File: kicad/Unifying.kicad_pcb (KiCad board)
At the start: 4 copper layers, 115.1 x 61 mm, 119 parts, among them J1 Conn_01x02, J10 HDMI_C_1.4, J11 HDMI_C_1.4, J12 nRpiBoot, J13 Conn_01x03, J14 Conn_01x03, J15 AudioOUT, J16 Micro_SD_Card_Det, J17 THD-20-R, J18 GLOBAL_EN, J19 AudioAMP, J2 Bus_M.2_Socket_B, J3 USB_OTG, J4 Conn_01x04_Male, J5 USB_A, J6 USB_A, J7 USB_MICRO, J8 Conn_01x22_Female, J9 Conn_01x22_Female, Q1 DMP3013SFV-7, U10 74LVC1G07SE-7, U11 RT9742GGJ5, U2 AP64501SP-13, U3 FSUSB42MUX, U4 USB2514B-I/M2, U6 AP22653W6, U7 RT9742SNGV, U8 74LVC1G07SE-7, U9 NC7WZ16, Y1 24MHz

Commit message: Adding changes to PCB, routing board
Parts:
- added R2: DNP, Resistor_SMD:R_0402_1005Metric, F.Cu at (123.3, 95.0)
- J10: value HDMI_C_1.4 -> GPDI0; footprint CM4IO:EDAC 690-019-298-412 -> hdmi-d:CONN-10029449-111RLF
- J11: value HDMI_C_1.4 -> GPDI1; footprint CM4IO:EDAC 690-019-298-412 -> hdmi-d:CONN-10029449-111RLF
- moved J11 2.65 mm to (128.4, 86.6)
- moved J10 1.81 mm to (104.5, 88.6)
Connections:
- net /CM4_HighSpeed/HDMI0_CK_N renamed HDMI0_CK_N
- net /CM4_HighSpeed/HDMI0_D0_N renamed HDMI0_D0_N
- net /CM4_HighSpeed/HDMI0_D1_N renamed HDMI0_D1_N
- net /CM4_HighSpeed/HDMI0_D2_N renamed HDMI0_D2_N
- net /CM4_HighSpeed/HDMI0_HOTPLUG renamed HDMI0_HOTPLUG
- net /CM4_HighSpeed/HDMI0_SCL renamed HDMI0_SCL
- net /CM4_HighSpeed/HDMI0_SDA renamed HDMI0_SDA
- net /CM4_HighSpeed/HDMI_5v renamed HDMI_5v
- J10 pad 1: GND -> HDMI0_D2_P
- J10 pad 10: GND -> HDMI0_CK_P
- J10 pad 11: /CM4_HighSpeed/HDMI0_CK_P -> GND
- J10 pad 13: GND -> HDMI0_CEC
- J10 pad 14: /CM4_HighSpeed/HDMI0_CEC -> unconnected-(J10-P14)
- J10 pad 17: unconnected-(J10-UTILITY/HEAC+) -> GND
- J10 pad 2: /CM4_HighSpeed/HDMI0_D2_P -> GND
- J10 pad 4: GND -> HDMI0_D1_P
- J10 pad 5: /CM4_HighSpeed/HDMI0_D1_P -> GND
- J10 pad 7: GND -> HDMI0_D0_P
- J10 pad 8: /CM4_HighSpeed/HDMI0_D0_P -> GND
- J11 pad 1: GND -> /CM4_HighSpeed/HDMI1_D2_P
- J11 pad 10: GND -> /CM4_HighSpeed/HDMI1_CK_P
- J11 pad 11: /CM4_HighSpeed/HDMI1_CK_P -> GND
- J11 pad 13: GND -> /CM4_HighSpeed/HDMI1_CEC
- J11 pad 14: /CM4_HighSpeed/HDMI1_CEC -> unconnected-(J11-P14)
- J11 pad 17: unconnected-(J11-UTILITY/HEAC+) -> GND
- J11 pad 2: /CM4_HighSpeed/HDMI1_D2_P -> GND
- J11 pad 4: GND -> /CM4_HighSpeed/HDMI1_D1_P
- J11 pad 5: /CM4_HighSpeed/HDMI1_D1_P -> GND
- J11 pad 7: GND -> /CM4_HighSpeed/HDMI1_D0_P
- J11 pad 8: /CM4_HighSpeed/HDMI1_D0_P -> GND
- J8 pad 1: GND -> /+3.3v
- J8 pad 11: unconnected-(J8-Pin_11) -> /CM4_HighSpeed/CAM1_D2_P
- J8 pad 12: unconnected-(J8-Pin_12) -> /CM4_HighSpeed/CAM1_D2_N
- J8 pad 14: unconnected-(J8-Pin_14) -> /CM4_HighSpeed/CAM1_C_P
- J8 pad 15: unconnected-(J8-Pin_15) -> /CM4_HighSpeed/CAM1_C_N
- J8 pad 17: /CM4_HighSpeed/CAM_GPIO -> /CM4_HighSpeed/CAM1_D1_P
- J8 pad 18: unconnected-(J8-Pin_18) -> /CM4_HighSpeed/CAM1_D1_N
- J8 pad 2: /CM4_HighSpeed/CAM1_D0_N -> /CM4_HighSpeed/SDA0
- J8 pad 20: /CM4_HighSpeed/SCL0 -> /CM4_HighSpeed/CAM1_D0_P
- J8 pad 21: /CM4_HighSpeed/SDA0 -> /CM4_HighSpeed/CAM1_D0_N
- J8 pad 22: /CM4_HighSpeed/+3.3v -> GND
- J8 pad 3: /CM4_HighSpeed/CAM1_D0_P -> /CM4_HighSpeed/SCL0
- J8 pad 5: /CM4_HighSpeed/CAM1_D1_N -> unconnected-(J8-Pin_5)
- J8 pad 6: /CM4_HighSpeed/CAM1_D1_P -> /CM4_HighSpeed/CAM_GPIO
- J8 pad 8: /CM4_HighSpeed/CAM1_C_N -> /CM4_HighSpeed/CAM1_D3_P
- J8 pad 9: /CM4_HighSpeed/CAM1_C_P -> /CM4_HighSpeed/CAM1_D3_N
- J9 pad 1: GND -> /+3.3v
- J9 pad 11: /CM4_HighSpeed/DSI1_D2_N -> /CM4_HighSpeed/DSI1_D2_P
- J9 pad 12: /CM4_HighSpeed/DSI1_D2_P -> /CM4_HighSpeed/DSI1_D2_N
- J9 pad 14: /CM4_HighSpeed/DSI1_D3_N -> /CM4_HighSpeed/DSI1_C_P
- J9 pad 15: /CM4_HighSpeed/DSI1_D3_P -> /CM4_HighSpeed/DSI1_C_N
- J9 pad 17: unconnected-(J9-Pin_17) -> /CM4_HighSpeed/DSI1_D1_P
- J9 pad 18: unconnected-(J9-Pin_18) -> /CM4_HighSpeed/DSI1_D1_N
- J9 pad 2: /CM4_HighSpeed/DSI1_D0_N -> /CM4_HighSpeed/SDA0
- J9 pad 20: /CM4_HighSpeed/SCL0 -> /CM4_HighSpeed/DSI1_D0_P
- J9 pad 21: /CM4_HighSpeed/SDA0 -> /CM4_HighSpeed/DSI1_D0_N
- J9 pad 22: /CM4_HighSpeed/+3.3v -> GND
- J9 pad 3: /CM4_HighSpeed/DSI1_D0_P -> /CM4_HighSpeed/SCL0
- J9 pad 5: /CM4_HighSpeed/DSI1_D1_N -> unconnected-(J9-Pin_5)
- J9 pad 6: /CM4_HighSpeed/DSI1_D1_P -> unconnected-(J9-Pin_6)
- J9 pad 8: /CM4_HighSpeed/DSI1_C_N -> /CM4_HighSpeed/DSI1_D3_P
- J9 pad 9: /CM4_HighSpeed/DSI1_C_P -> /CM4_HighSpeed/DSI1_D3_N
- Module1 pad 151: /CM4_HighSpeed/HDMI0_CEC -> HDMI0_CEC
- Module1 pad 170: /CM4_HighSpeed/HDMI0_D2_P -> HDMI0_D2_P
- Module1 pad 176: /CM4_HighSpeed/HDMI0_D1_P -> HDMI0_D1_P
- Module1 pad 182: /CM4_HighSpeed/HDMI0_D0_P -> HDMI0_D0_P
- Module1 pad 188: /CM4_HighSpeed/HDMI0_CK_P -> HDMI0_CK_P
- Module1 pad 80: /CM4_GPIO (GPIO, SDCARD)/SCL0 -> /CM4_HighSpeed/SCL0
- Module1 pad 82: /CM4_GPIO (GPIO, SDCARD)/SDA0 -> /CM4_HighSpeed/SDA0
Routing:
- net HDMI0_D2_P: track 0.00 -> 56.9 mm
- net HDMI0_D1_P: track 0.00 -> 56.3 mm
- net HDMI0_D0_P: track 0.00 -> 55.3 mm
- net /CM4_HighSpeed/HDMI0_D2_P: track 55.0 -> 0.00 mm
- net /CM4_HighSpeed/HDMI0_D1_P: track 54.4 -> 0.00 mm
- net HDMI0_CK_P: track 0.00 -> 54.0 mm
- net /CM4_HighSpeed/HDMI0_D0_P: track 53.3 -> 0.00 mm
- net /CM4_HighSpeed/HDMI0_CK_P: track 52.0 -> 0.00 mm
- net HDMI0_CEC: track 0.00 -> 48.5 mm, vias 0 -> 2
- net /CM4_HighSpeed/HDMI0_CEC: track 46.5 -> 0.00 mm, vias 2 -> 0
- net /CM4_HighSpeed/SDA0: track 21.6 -> 63.4 mm, vias 0 -> 5
- net /CM4_HighSpeed/SCL0: track 22.8 -> 63.0 mm, vias 0 -> 3
- net /CM4_HighSpeed/CAM1_D3_P: track 0.00 -> 37.4 mm, vias 0 -> 1
- net /CM4_HighSpeed/CAM1_D3_N: track 0.00 -> 37.2 mm, vias 0 -> 1
- net /CM4_HighSpeed/CAM1_D2_P: track 0.00 -> 34.8 mm, vias 0 -> 1
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
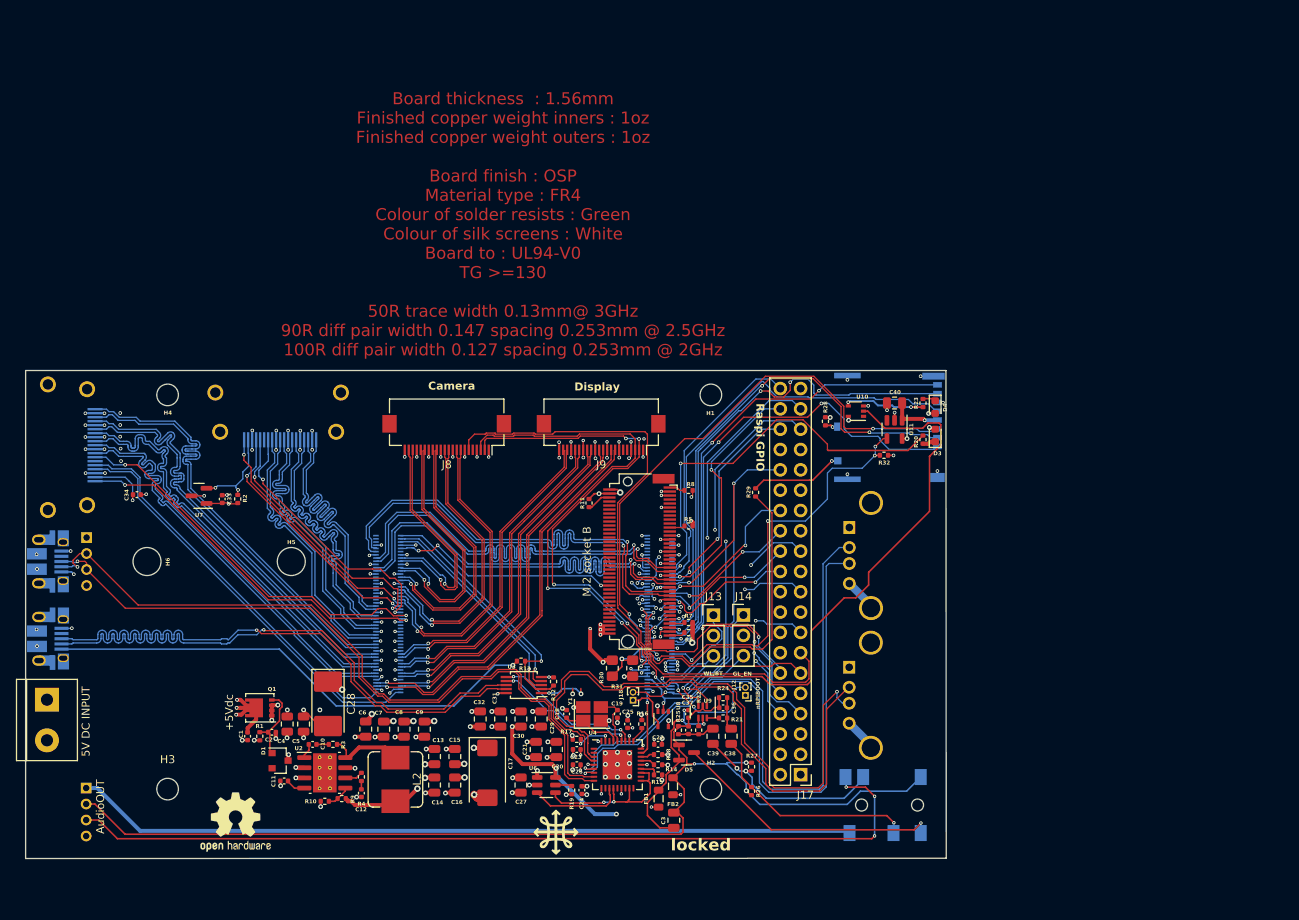
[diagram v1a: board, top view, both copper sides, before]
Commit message: Adding I2C poullups to schematics
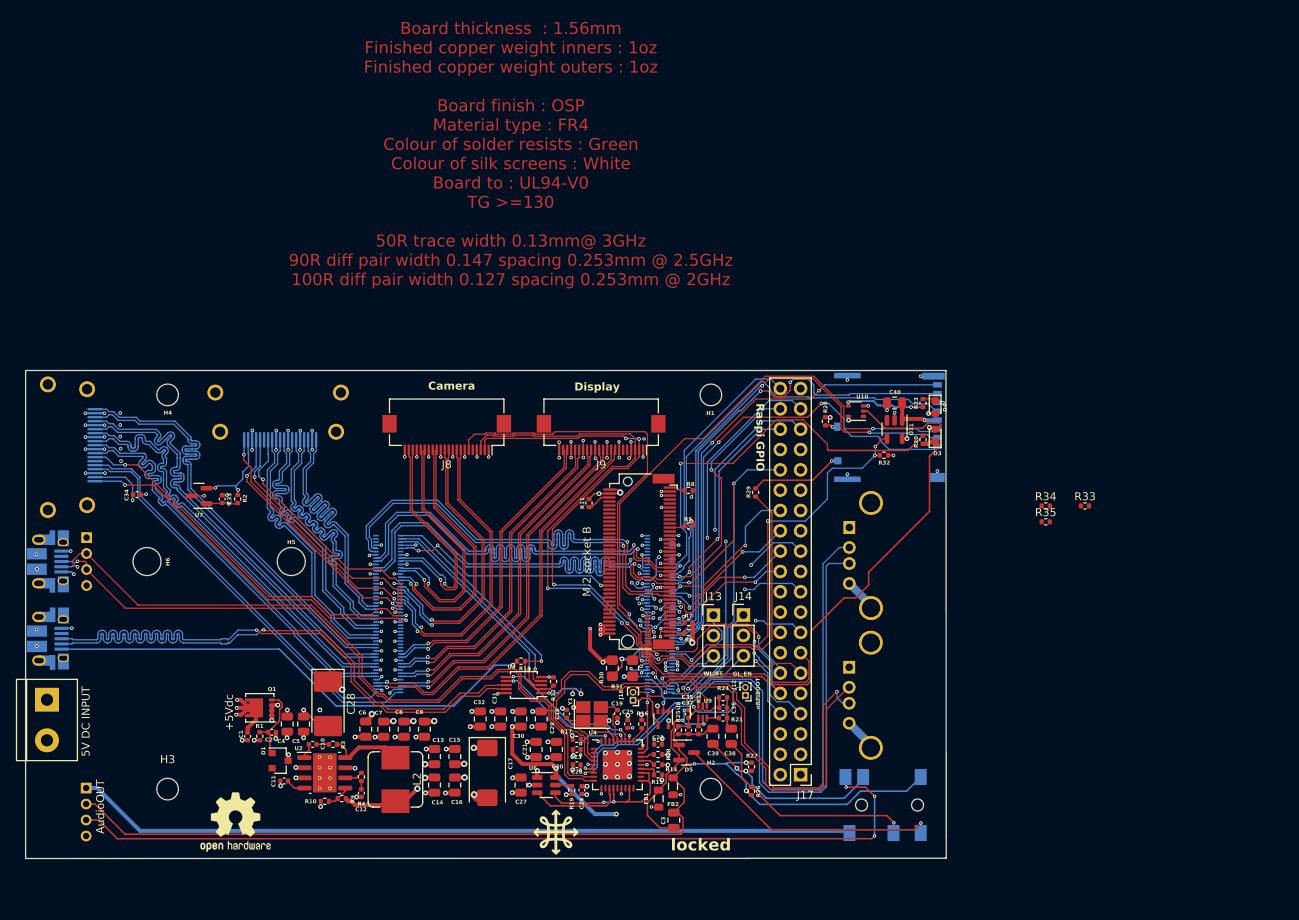
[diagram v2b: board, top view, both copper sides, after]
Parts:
- added R33: DNP, Resistor_SMD:R_0402_1005Metric, F.Cu at (229.2, 95.9)
- added R34: 4K7, Resistor_SMD:R_0402_1005Metric, F.Cu at (224.3, 95.9)
- added R35: 4K7, Resistor_SMD:R_0402_1005Metric, F.Cu at (224.3, 97.9)
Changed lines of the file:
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@@
     )
   )
+  (footprint "Resistor_SMD:R_0402_1005Metric" (layer "F.Cu")
+    (at 229.25 95.91)
+    (descr "Resistor SMD 0402 (1005 Metric), square (rectangular) end terminal, IPC_7351 nominal, (Body size source: IPC-SM-782 page 72, https://www.pcb-3d.com/wordpress/wp-content/uploads/ipc-sm-782a_amendment_1_and_2.pdf), generated with kicad-footprint-generator")
+    (tags "resistor")
+    (property "Sheetfile" "File: CM4_GPIO.kicad_sch")
+    (property "Sheetname" "CM4_GPIO (GPIO, SDCARD)")
+    (property "ki_description" "Resistor, small symbol")
+    (property "ki_keywords" "R resistor")
+    (attr smd)
+    (fp_text reference "R33" (at 0 -1.17) (layer "F.SilkS")
+        (effects (font (size 1 1) (thickness 0.15)))
+    )
+    (fp_text value "DNP" (at 0 1.17) (layer "F.Fab")
+        (effects (font (size 1 1) (thickness 0.15)))
+    )
+    (fp_text user "${REFERENCE}" (at 0 0) (layer "F.Fab")
+        (effects (font (size 0.26 0.26) (thickness 0.04)))
+    )
+    (fp_line (start -0.153641 -0.38) (end 0.153641 -0.38)
+      (stroke (width 0.12) (type solid)) (layer "F.SilkS"))
+    (fp_line (start -0.153641 0.38) (end 0.153641 0.38)
+      (stroke (width 0.12) (type solid)) (layer "F.SilkS"))
+    (fp_line (start -0.93 -0.47) (end 0.93 -0.47)
+      (stroke (width 0.05) (type solid)) (layer "F.CrtYd"))
+    (fp_line (start -0.93 0.47) (end -0.93 -0.47)
+      (stroke (width 0.05) (type solid)) (layer "F.CrtYd"))
+    (fp_line (start 0.93 -0.47) (end 0.93 0.47)
+      (stroke (width 0.05) (type solid)) (layer "F.CrtYd"))
+    (fp_line (start 0.93 0.47) (end -0.93 0.47)
+      (stroke (width 0.05) (type solid)) (layer "F.CrtYd"))
+    (fp_line (start -0.525 -0.27) (end 0.525 -0.27)
+      (stroke (width 0.1) (type solid)) (layer "F.Fab"))
+    (fp_line (start -0.525 0.27) (end -0.525 -0.27)
+      (stroke (width 0.1) (type solid)) (layer "F.Fab"))
+    (fp_line (start 0.525 -0.27) (end 0.525 0.27)
+      (stroke (width 0.1) (type solid)) (layer "F.Fab"))
+    (fp_line (start 0.525 0.27) (end -0.525 0.27)
+      (stroke (width 0.1) (type solid)) (layer "F.Fab"))
+    (pad "1" smd roundrect (at -0.51 0) (size 0.54 0.64) (layers "F.Cu" "F.Paste" "F.Mask") (roundrect_rratio 0.25)
+      (net 42 "/CM4_GPIO (GPIO, SDCARD)/SD_PWR") (pintype "passive"))
+    (pad "2" smd roundrect (at 0.51 0) (size 0.54 0.64) (layers "F.Cu" "F.Paste" "F.Mask") (roundrect_rratio 0.25)
+      (net 94 "/+3.3v") (pintype "passive"))
+    (model "${KICAD6_3DMODEL_DIR}/Resistor_SMD.3dshapes/R_0402_1005Metric.wrl"
+      (offset (xyz 0 0 0))
+      (scale (xyz 1 1 1))
+      (rotate (xyz 0 0 0))
+    )
+  )
   (footprint "Capacitor_SMD:C_0805_2012Metric" (layer "F.Cu")
     (at 139.34 123.81 90)
@@
     )
   )
+  (footprint "Resistor_SMD:R_0402_1005Metric" (layer "F.Cu")
+    (at 224.34 95.91)
+    (descr "Resistor SMD 0402 (1005 Metric), square (rectangular) end terminal, IPC_7351 nominal, (Body size source: IPC-SM-782 page 72, https://www.pcb-3d.com/wordpress/wp-content/uploads/ipc-sm-782a_amendment_1_and_2.pdf), generated with kicad-footprint-generator")
+    (tags "resistor")
+    (property "Sheetfile" "File: CM4_HighSpeed.kicad_sch")
+    (property "Sheetname" "CM4_HighSpeed")
+    (property "ki_description" "Resistor, small symbol")
+    (property "ki_keywords" "R resistor")
+    (attr smd)
+    (fp_text reference "R34" (at 0 -1.17) (layer "F.SilkS")
+        (effects (font (size 1 1) (thickness 0.15)))
+    )
+    (fp_text value "4K7" (at 0 1.17) (layer "F.Fab")
+        (effects (font (size 1 1) (thickness 0.15)))
+    )
+    (fp_text user "${REFERENCE}" (at 0 0) (layer "F.Fab")
+        (effects (font (size 0.26 0.26) (thickness 0.04)))
+    )
+    (fp_line (start -0.153641 -0.38) (end 0.153641 -0.38)
+      (stroke (width 0.12) (type solid)) (layer "F.SilkS"))
+    (fp_line (start -0.153641 0.38) (end 0.153641 0.38)
+      (stroke (width 0.12) (type solid)) (layer "F.SilkS"))
+    (fp_line (start -0.93 -0.47) (end 0.93 -0.47)
+      (stroke (width 0.05) (type solid)) (layer "F.CrtYd"))
+    (fp_line (start -0.93 0.47) (end -0.93 -0.47)
+      (stroke (width 0.05) (type solid)) (layer "F.CrtYd"))
+    (fp_line (start 0.93 -0.47) (end 0.93 0.47)
+      (stroke (width 0.05) (type solid)) (layer "F.CrtYd"))
+    (fp_line (start 0.93 0.47) (end -0.93 0.47)
+      (stroke (width 0.05) (type solid)) (layer "F.CrtYd"))
+    (fp_line (start -0.525 -0.27) (end 0.525 -0.27)
+      (stroke (width 0.1) (type solid)) (layer "F.Fab"))
+    (fp_line (start -0.525 0.27) (end -0.525 -0.27)
+      (stroke (width 0.1) (type solid)) (layer "F.Fab"))
+    (fp_line (start 0.525 -0.27) (end 0.525 0.27)
+      (stroke (width 0.1) (type solid)) (layer "F.Fab"))
+    (fp_line (start 0.525 0.27) (end -0.525 0.27)
+      (stroke (width 0.1) (type solid)) (layer "F.Fab"))
+    (pad "1" smd roundrect (at -0.51 0) (size 0.54 0.64) (layers "F.Cu" "F.Paste" "F.Mask") (roundrect_rratio 0.25)
+      (net 94 "/+3.3v") (pintype "passive"))
+    (pad "2" smd roundrect (at 0.51 0) (size 0.54 0.64) (layers "F.Cu" "F.Paste" "F.Mask") (roundrect_rratio 0.25)
+      (net 108 "/CM4_HighSpeed/SCL0") (pintype "passive"))
+    (model "${KICAD6_3DMODEL_DIR}/Resistor_SMD.3dshapes/R_0402_1005Metric.wrl"
+      (offset (xyz 0 0 0))
+      (scale (xyz 1 1 1))
+      (rotate (xyz 0 0 0))
+    )
+  )
   (footprint "MountingHole:M.2Hole_3.5mm" (layer "F.Cu")
     (at 130.033 102.86)
@@
     )
   )
+  (footprint "Resistor_SMD:R_0402_1005Metric" (layer "F.Cu")
+    (at 224.34 97.9)
+    (descr "Resistor SMD 0402 (1005 Metric), square (rectangular) end terminal, IPC_7351 nominal, (Body size source: IPC-SM-782 page 72, https://www.pcb-3d.com/wordpress/wp-content/uploads/ipc-sm-782a_amendment_1_and_2.pdf), generated with kicad-footprint-generator")
+    (tags "resistor")
+    (property "Sheetfile" "File: CM4_HighSpeed.kicad_sch")
+    (property "Sheetname" "CM4_HighSpeed")
+    (property "ki_description" "Resistor, small symbol")
+    (property "ki_keywords" "R resistor")
+    (attr smd)
+    (fp_text reference "R35" (at 0 -1.17) (layer "F.SilkS")
+        (effects (font (size 1 1) (thickness 0.15)))
+    )
+    (fp_text value "4K7" (at 0 1.17) (layer "F.Fab")
+        (effects (font (size 1 1) (thickness 0.15)))
+    )
+    (fp_text user "${REFERENCE}" (at 0 0) (layer "F.Fab")
+        (effects (font (size 0.26 0.26) (thickness 0.04)))
+    )
+    (fp_line (start -0.153641 -0.38) (end 0.153641 -0.38)
+      (stroke (width 0.12) (type solid)) (layer "F.SilkS"))
+    (fp_line (start -0.153641 0.38) (end 0.153641 0.38)
+      (stroke (width 0.12) (type solid)) (layer "F.SilkS"))
+    (fp_line (start -0.93 -0.47) (end 0.93 -0.47)
+      (stroke (width 0.05) (type solid)) (layer "F.CrtYd"))
+    (fp_line (start -0.93 0.47) (end -0.93 -0.47)
+      (stroke (width 0.05) (type solid)) (layer "F.CrtYd"))
+    (fp_line (start 0.93 -0.47) (end 0.93 0.47)
+      (stroke (width 0.05) (type solid)) (layer "F.CrtYd"))
+    (fp_line (start 0.93 0.47) (end -0.93 0.47)
+      (stroke (width 0.05) (type solid)) (layer "F.CrtYd"))
+    (fp_line (start -0.525 -0.27) (end 0.525 -0.27)
+      (stroke (width 0.1) (type solid)) (layer "F.Fab"))
+    (fp_line (start -0.525 0.27) (end -0.525 -0.27)
+      (stroke (width 0.1) (type solid)) (layer "F.Fab"))
+    (fp_line (start 0.525 -0.27) (end 0.525 0.27)
+      (stroke (width 0.1) (type solid)) (layer "F.Fab"))
+    (fp_line (start 0.525 0.27) (end -0.525 0.27)
+      (stroke (width 0.1) (type solid)) (layer "F.Fab"))
+    (pad "1" smd roundrect (at -0.51 0) (size 0.54 0.64) (layers "F.Cu" "F.Paste" "F.Mask") (roundrect_rratio 0.25)
+      (net 94 "/+3.3v") (pintype "passive"))
+    (pad "2" smd roundrect (at 0.51 0) (size 0.54 0.64) (layers "F.Cu" "F.Paste" "F.Mask") (roundrect_rratio 0.25)
+      (net 109 "/CM4_HighSpeed/SDA0") (pintype "passive"))
+    (model "${KICAD6_3DMODEL_DIR}/Resistor_SMD.3dshapes/R_0402_1005Metric.wrl"
+      (offset (xyz 0 0 0))
+      (scale (xyz 1 1 1))
+      (rotate (xyz 0 0 0))
+    )
+  )
   (footprint "Capacitor_SMD:C_0402_1005Metric" (layer "F.Cu")
     (at 179.69 121.91 -90)
@@
   (gr_line (start 96.8202 139.986) (end 211.9 139.95)
     (stroke (width 0.05) (type solid)) (layer "Edge.Cuts"))
-  (gr_text "Board thickness  : 1.56mm\nFinished copper weight inners : 1oz\nFinished copper weight outers : 1oz\n\nBoard finish : OSP\nMaterial type : FR4\nColour of solder resists : Green\nColour of silk screens : White\nBoard to : UL94-V0\nTG >=130\n\n50R trace width 0.13mm@ 3GHz\n90R diff pair width 0.147 spacing 0.253mm @ 2.5GHz\n100R diff pair width 0.127 spacing 0.253mm @ 2GHz" (at 156.5 60.7) (layer "F.Cu")
+  (gr_text "Board thickness  : 1.56mm\nFinished copper weight inners : 1oz\nFinished copper weight outers : 1oz\n\nBoard finish : OSP\nMaterial type : FR4\nColour of solder resists : Green\nColour of silk screens : White\nBoard to : UL94-V0\nTG >=130\n\n50R trace width 0.13mm@ 3GHz\n90R diff pair width 0.147 spacing 0.253mm @ 2.5GHz\n100R diff pair width 0.127 spacing 0.253mm @ 2GHz" (at 157.48 51.92) (layer "F.Cu")
     (effects (font (size 1.5 1.5) (thickness 0.3)))
   )

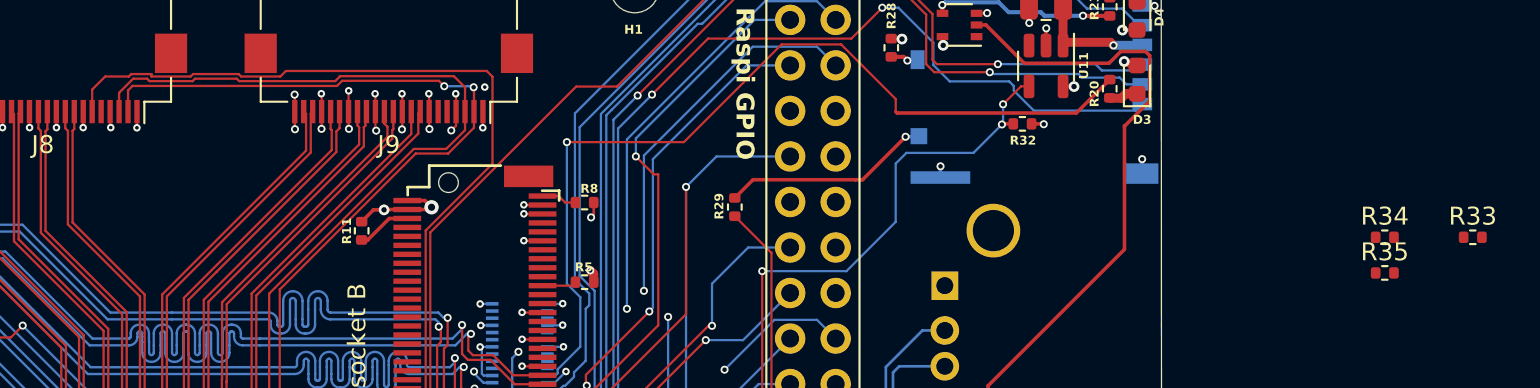
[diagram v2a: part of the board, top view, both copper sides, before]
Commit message: Adding I2C resistors on PCB - routing fix 4
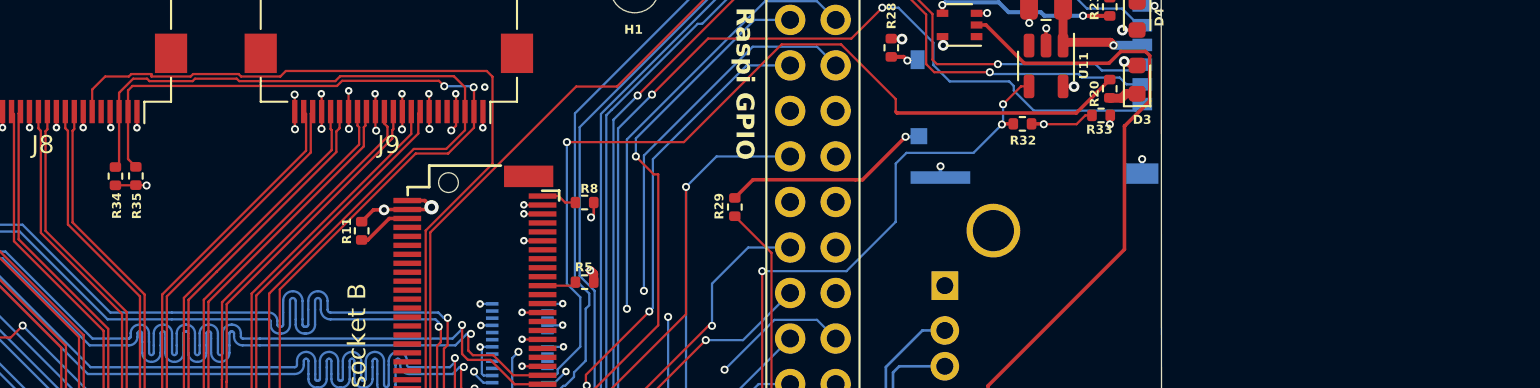
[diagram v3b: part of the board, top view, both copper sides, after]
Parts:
- moved R34 70.9 mm to (153.5, 92.5), turned to 90 degrees
- moved R35 69.9 mm to (154.7, 92.5), turned to 90 degrees
- moved R33 21.8 mm to (208.5, 89.1), turned to 180 degrees
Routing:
- net /CM4_GPIO (GPIO, SDCARD)/SD_PWR: track 6.74 -> 16.2 mm, vias 1 -> 2
- net /+3.3v: track 283.2 -> 289.9 mm, vias 29 -> 30
- net /CM4_HighSpeed/SDA0: track 63.4 -> 66.7 mm
- net /CM4_HighSpeed/SCL0: track 63.0 -> 66.2 mm

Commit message: Adding ethernet connector to schematics
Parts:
- added C41: 100n, Capacitor_SMD:C_0402_1005Metric, F.Cu at (240.3, 90.2)
- added J20: THD-02-R, Connector_PinHeader_2.54mm:PinHeader_2x02_P2.54mm_Vertical, F.Cu at (234.0, 91.6)
- added R36: 470R, Resistor_SMD:R_0402_1005Metric, F.Cu at (238.9, 97.4)
- added R37: 470R, Resistor_SMD:R_0402_1005Metric, F.Cu at (238.9, 99.4)
- added U1: TPD4EUSB30, Package_SON:USON-10_2.5x1.0mm_P0.5mm, F.Cu at (233.1, 98.5)
- added U12: MagJack-A70-112-331N126, CM4IO:TRJG0926HENL, F.Cu at (242.8, 115.9)
- added U5: TPD4EUSB30, Package_SON:USON-10_2.5x1.0mm_P0.5mm, F.Cu at (236.0, 98.5)
